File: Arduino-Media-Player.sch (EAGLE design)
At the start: 40 parts, among them IC1 AMS117-18, IC2 AMS117-33, U1 VS1053B, U2 FT232RLSSOP, U3 ATMEGA328P, U4 DS1307SO8, U5 74HC4050 LVL CONVERTER

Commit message: More minor changes
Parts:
- removed IC1: AMS117-18, SparkFun-PowerIC:V_REG_LM1117SOT223
- removed IC2: AMS117-33, SparkFun-PowerIC:V_REG_LM1117SOT223
- added U$1: MICRO-SD-CARD-EBAY, SparkFun-Connectors:MICRO-SD-CARD-EBAY
- added U6: VS1053B, SparkFun-DigitalIC:VS1033/1053SMD
- added U7: 74HC4050 LVL CONVERTER, SparkFun-DigitalIC:HEX_CONVERTER
- U1: value VS1053B -> ATMEGA328P; device SparkFun-DigitalIC:VS1033/1053SMD -> SparkFun-DigitalIC:ATMEGA328_SMT
- U3: value ATMEGA328P -> DS1307SO8; device SparkFun-DigitalIC:ATMEGA328_SMT -> SparkFun-FreqCtrl:DS1307SO8
- U4: value DS1307SO8 -> AMS117-33; device SparkFun-FreqCtrl:DS1307SO8 -> SparkFun-PowerIC:V_REG_LM1117SOT223
- U5: value 74HC4050 LVL CONVERTER -> AMS117-18; device SparkFun-DigitalIC:HEX_CONVERTER -> SparkFun-PowerIC:V_REG_LM1117SOT223
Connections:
- net /RESET: now also U1.PC6(/RESET); no longer U3.PC6(/RESET)
- net 1.8V: now also U5.OUT, U5.OUT@1, U6.CVDD1, U6.CVDD2, U6.CVDD3, U6.CVDD4; no longer IC1.OUT, IC1.OUT@1, U1.CVDD1, U1.CVDD2, U1.CVDD3, U1.CVDD4
- net 3.3V: now also U4.OUT, U4.OUT@1, U5.IN, U6.AVDD1, U6.AVDD2, U6.AVDD3, U6.IOVDD1, U6.IOVDD2, U6.IOVDD3, U6.TEST, U7.VCC; no longer IC1.IN, IC2.OUT, IC2.OUT@1, U1.AVDD1, U1.AVDD2, U1.AVDD3, U1.IOVDD1, U1.IOVDD2, U1.IOVDD3, U1.TEST, U5.VCC
- net 5V: now also U1.AREF, U1.AVCC, U1.VCC@1, U1.VCC@2, U3.VCC, U4.IN; no longer IC2.IN, U3.AREF, U3.AVCC, U3.VCC@1, U3.VCC@2, U4.VCC
- net 5V-MOSI: now also U7.1A; no longer U5.1A
- net 5V-MP3-CS: now also U7.4A; no longer U5.4A
- net 5V-MP3-DCS: now also U7.5A; no longer U5.5A
- net 5V-MP3-RST: now also U7.6A; no longer U5.6A
- net 5V-SCK: now also U7.3A; no longer U5.3A
- net 5V-SD-CS: now also U7.2A; no longer U5.2A
- net DS1307X1: now also U3.X1; no longer U4.X1
- net DS1307X2: now also U3.X2; no longer U4.X2
- net GBUF: now also U6.GBUF; no longer U1.GBUF
- net GND: now also U1.AGND, U1.GND@1, U1.GND@2, U3.GND, U4.ADJ, U5.ADJ, U6.AGND1, U6.AGND2, U6.AGND3, U6.AGND4, U6.DGND1, U6.DGND2, U6.DGND3, U6.DGND4, U6.DGND5, U6.DGND6, U7.GND; no longer IC1.ADJ, IC2.ADJ, U1.AGND1, U1.AGND2, U1.AGND3, U1.AGND4, U1.DGND1, U1.DGND2, U1.DGND3, U1.DGND4, U1.DGND5, U1.DGND6, U3.AGND, U3.GND@1, U3.GND@2, U4.GND, U5.GND
- net GPIO0: now also U6.GPIO0/I2S_SCLK; no longer U1.GPIO0/I2S_SCLK
- net GPIO1: now also U6.GPIO1/I2S_SDATA; no longer U1.GPIO1/I2S_SDATA
- net LEFT: now also U6.LEFT; no longer U1.LEFT
- net MIDI-RX: now also U6.RX; no longer U1.RX
- net MISO: now also U1.PB4(MISO), U6.S0; no longer U1.S0, U3.PB4(MISO)
- net MOSI: now also U6.SI, U7.1Y; no longer U1.SI, U5.1Y
- net MP3-CS: now also U6.XCS, U7.4Y; no longer U1.XCS, U5.4Y
- net MP3-DCS: now also U6.XDCS/BSYNC, U7.5Y; no longer U1.XDCS/BSYNC, U5.5Y
- net MP3-DREQ: now also U6.DREQ; no longer U1.DREQ
- net MP3-RST: now also U6.XRESET, U7.6Y; no longer U1.XRESET, U5.6Y
- net N$12: now also U6.GPIO5/I2C_MCLK; no longer U1.GPIO5/I2C_MCLK
- net N$13: now also U6.GPIO4/I2S_LROUT; no longer U1.GPIO4/I2S_LROUT
- net N$16: now also U6.GPIO2/DCLK, U6.GPIO3/SDATA, U6.GPIO6, U6.GPIO7; no longer U1.GPIO2/DCLK, U1.GPIO3/SDATA, U1.GPIO6, U1.GPIO7
- net N$4: now also U1.PB6(XTAL1/TOSC1); no longer U3.PB6(XTAL1/TOSC1)
- net N$5: now also U1.PB7(XTAL2/TOSC2); no longer U3.PB7(XTAL2/TOSC2)
- net RCAP: now also U6.RCAP; no longer U1.RCAP
- net RIGHT: now also U6.RIGHT; no longer U1.RIGHT
- net RXD: now also U1.PD0(RXD); no longer U3.PD0(RXD)
- net SCK: now also U6.SCLK, U7.3Y; no longer U1.SCLK, U5.3Y
- net SCL: now also U1.PC5(ADC5/SCL), U3.SCL; no longer U3.PC5(ADC5/SCL), U4.SCL
- net SD-CS: now also U7.2Y; no longer U5.2Y
- net SDA: now also U1.PC4(ADC4/SDA), U3.SDA; no longer U3.PC4(ADC4/SDA), U4.SDA
- net SQW: now also U3.SQW; no longer U4.SQW
- net TXD: now also U1.PD1(TXD); no longer U3.PD1(TXD)
- net VBATT: now also U3.VBATT; no longer U4.VBATT
- net VS1053XTAL1: now also U6.XTAL1/MCLK; no longer U1.XTAL1/MCLK
- net VS1053XTAL2: now also U6.XTAL2; no longer U1.XTAL2
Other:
- note added: "ATMEGA328P-AU (Arduino)"
- note added: "Real-Time Clock (RTC)"
- note added: "USB-to-Serial"
- moved on the sheet: C103, C108, C109, R101, R103, R104, R112, XTAL3

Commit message: update
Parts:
- removed U$1: MICRO-SD-CARD-EBAY, SparkFun-Connectors:MICRO-SD-CARD-EBAY
- added J1: MICRO-SD-CARD, SparkFun-Connectors-EDITED:MICRO-SD-CARD-EBAY
- added R102, R105, R110, R111: 100K, SparkFun-Passives:RESISTOR0805-RES
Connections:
- net 3.3V: now also J1.VCC, R102.2, R105.2
- net GND: now also J1.GND, J1.SHEILD1, J1.SHEILD2, J1.SHEILD3, J1.SHEILD4, R110.1, R111.1
- net GPIO0: now also R111.2
- net GPIO1: now also R110.2
- net MIDI-RX: now also R102.1
- net MISO: now also J1.D0
- net MOSI: now also J1.D1
- net MP3-RST: now also R105.1
- net SCK: now also J1.SCK
- net SD-CS: now also J1.CS
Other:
- moved on the sheet: C103, C108, C109, R101, R103, R104, R112, U6, XTAL3

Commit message: update
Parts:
- removed R10: 10K, rcl:R-US_R0805W
- added R5: 10K, SparkFun-Passives:RESISTOR0805-RES
- PTC1: device SparkFun-Passives:RESISTOR0805-RES -> SparkFun-Passives:PTC
- R1, R2: device rcl:R-US_R0805W -> SparkFun-Passives:RESISTOR0805-RES
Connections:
- net /RESET: now also R5.1; no longer R10.1
- net 5V: now also R5.2; no longer R10.2

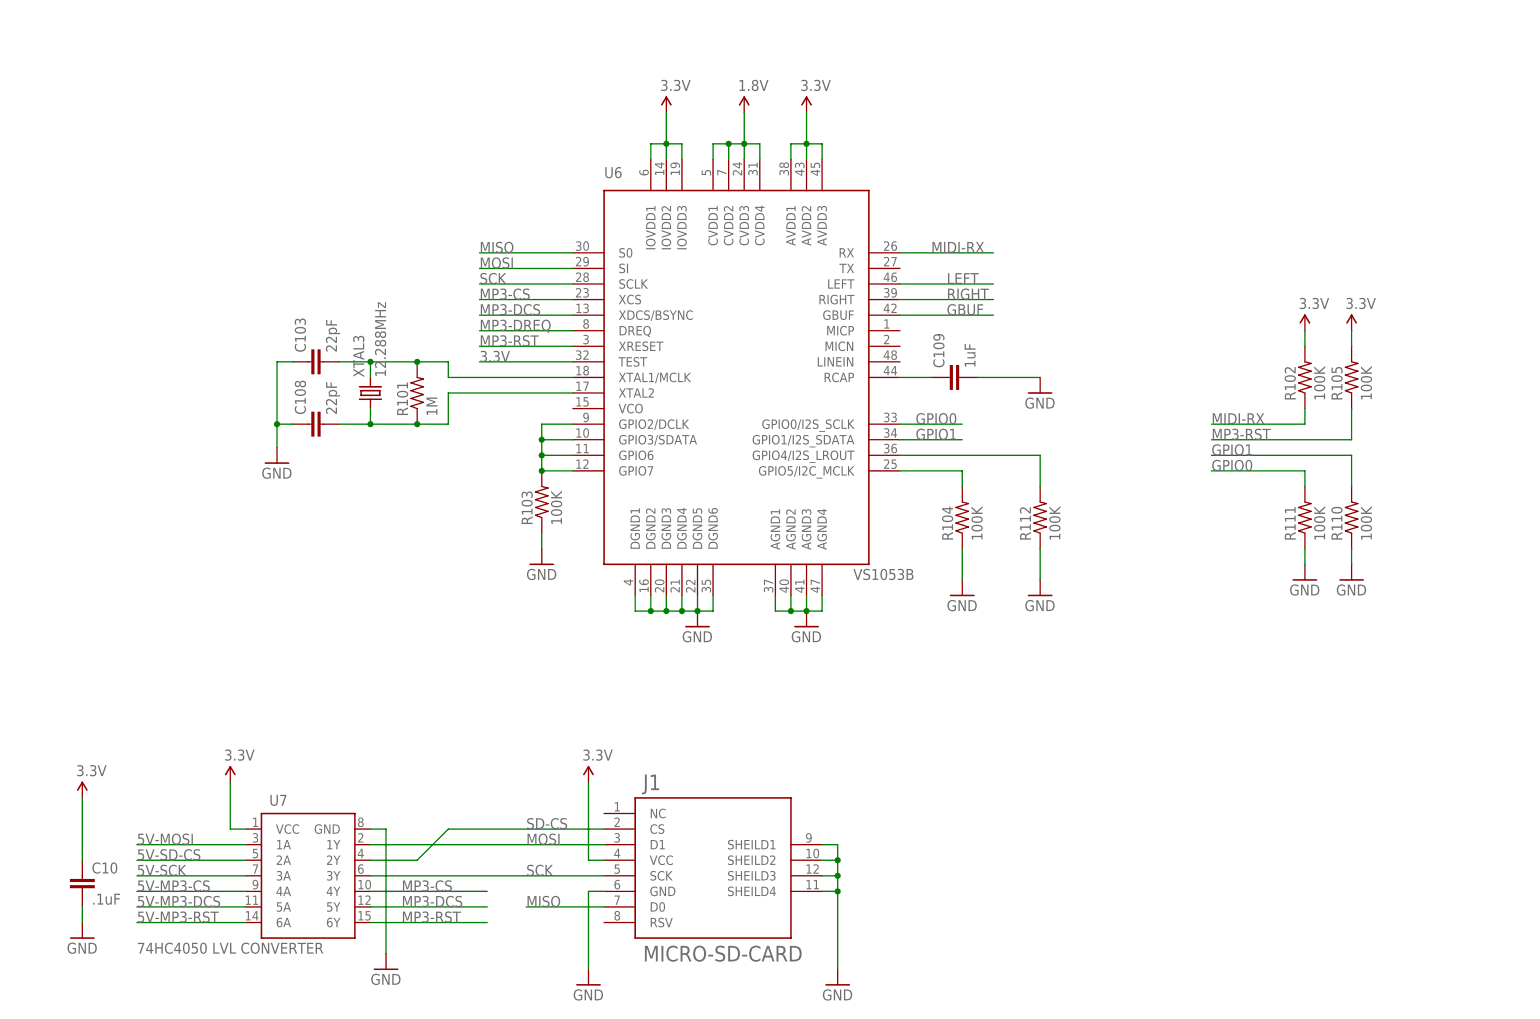
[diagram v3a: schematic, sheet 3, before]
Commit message: Added audio output circuitry for mp3 decoder
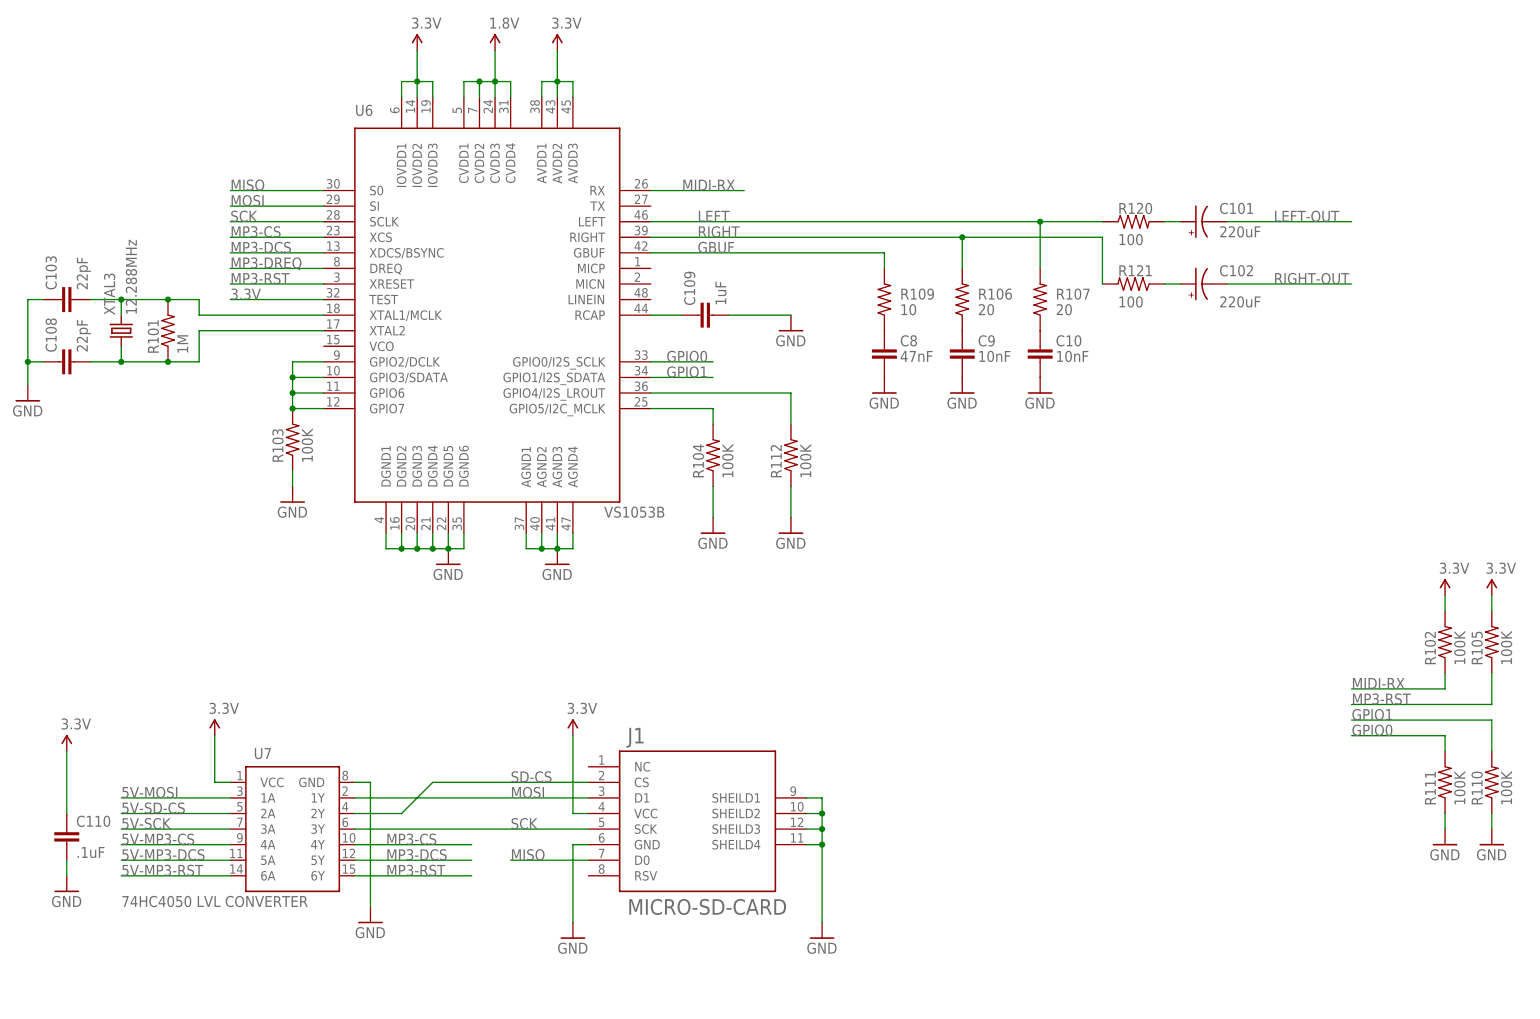
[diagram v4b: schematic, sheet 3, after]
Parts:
- added C101, C102: 220uF, SparkFun-Passives:CAP_POLG
- added C110: .1uF, SparkFun-Passives:CAP0805
- added C8: 47nF, SparkFun-Passives:CAP0805
- added C9: 10nF, SparkFun-Passives:CAP0805
- added R106, R107: 20, SparkFun-Passives:RESISTOR0805-RES
- added R109: 10, SparkFun-Passives:RESISTOR0805-RES
- added R120, R121: 100, SparkFun-Passives:RESISTOR0805-RES
- added R13, R14: 1K, SparkFun-Passives:RESISTOR0805-RES
- added SJ1, SJ2: JUMPER-PAD-2-NOROUND, SparkFun-Passives:JUMPER-PAD-2-NOROUND
- C10: value .1uF -> 10nF
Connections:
- new net 5V-GPIO1: SJ2.1, U1.PD4(XCK/T0)
- new net 5V-MIDI-RX: SJ1.1, U1.PD3(INT1)
- new net A0: U1.PC0(ADC0)
- new net A1: U1.PC1(ADC1)
- new net A2: U1.PC2(ADC2)
- new net A3: U1.PC3(ADC3)
- new net A6: U1.ADC6
- new net A7: U1.ADC7
- new net LEFT-OUT: C101.-
- new net N$1: R13.1, SJ1.2
- new net N$14: C102.+, R121.1
- new net N$15: C8.2, R109.1
- new net N$17: C9.2, R106.1
- new net N$18: C10.2, R107.1
- new net N$2: R14.1, SJ2.2
- new net N$3: C101.+, R120.2
- new net RIGHT-OUT: C102.-
- net 3.3V: now also C110.1; no longer C10.1
- net 5V-MOSI: now also U1.PB3(MOSI/OC2)
- net 5V-MP3-CS: now also U1.PD6(AIN0)
- net 5V-MP3-DCS: now also U1.PD7(AIN1)
- net 5V-MP3-RST: now also U1.PB0(ICP)
- net 5V-SCK: now also U1.PB5(SCK)
- net 5V-SD-CS: now also U1.PB1(OC1A)
- net GBUF: now also R109.2
- net GND: now also C10.1, C110.2, C8.1, C9.1; no longer C10.2
- net GPIO1: now also R14.2
- net LEFT: now also R107.2, R120.1
- net MIDI-RX: now also R13.2
- net MP3-DREQ: now also U1.PD2(INT0)
- net RIGHT: now also R106.2, R121.2
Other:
- moved on the sheet: C1, C10, C103, C108, C109, C12, C2, J1, R1, R101, R102, R103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

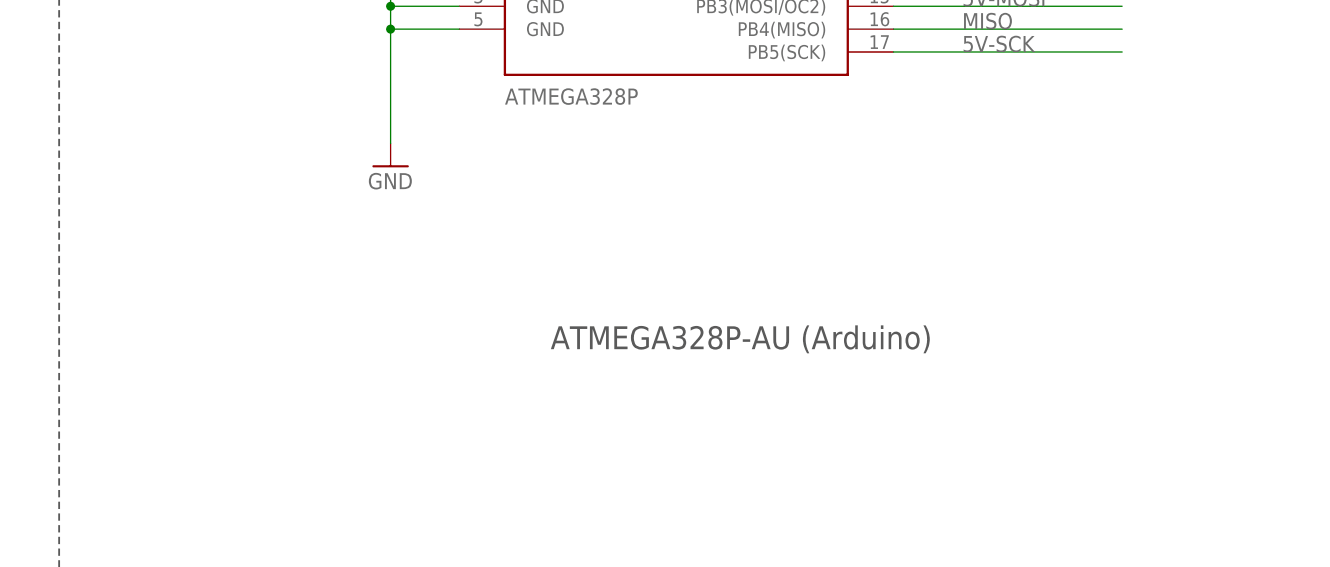
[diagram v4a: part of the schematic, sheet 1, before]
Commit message: Added ICSP header for ATMEGA328p
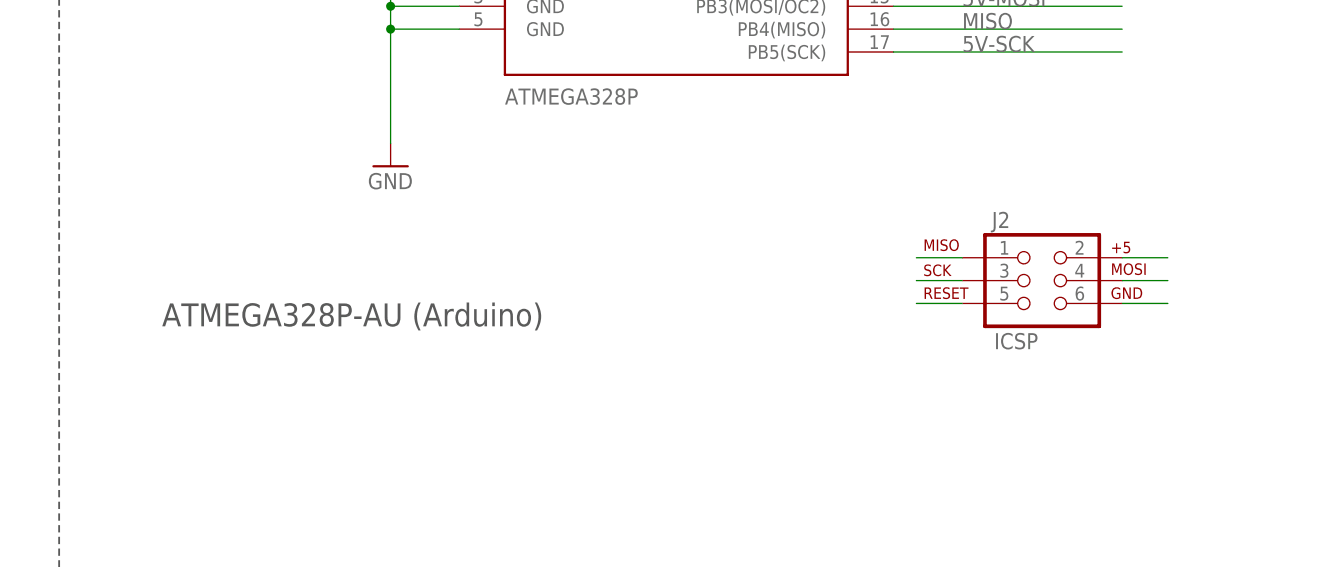
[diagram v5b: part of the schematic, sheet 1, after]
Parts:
- added J2: ICSP, SparkFun-Connectors-EDITED:AVR_SPI_PRG_6PTH
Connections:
- net /RESET: now also J2.5
- net 5V: now also J2.2
- net 5V-MOSI: now also J2.4
- net 5V-SCK: now also J2.3
- net GND: now also J2.6
- net MISO: now also J2.1
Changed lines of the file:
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@@
 <part name="GND27" library="SparkFun-Aesthetics" deviceset="GND" device=""/>
 <part name="GND28" library="SparkFun-Aesthetics" deviceset="GND" device=""/>
+<part name="J2" library="SparkFun-Connectors-EDITED" deviceset="AVR_SPI_PRG_6" device="PTH" value="ICSP"/>
 </parts>
 <sheets>
@@
 <text x="48.26" y="92.71" size="2.54" layer="97" ratio="15">USB-to-Serial</text>
 <text x="31.75" y="5.08" size="2.54" layer="97" ratio="15">Real-Time Clock (RTC)</text>
-<text x="172.72" y="33.02" size="2.54" layer="97" ratio="15">ATMEGA328P-AU (Arduino)</text>
+<text x="129.54" y="35.56" size="2.54" layer="97" ratio="15">ATMEGA328P-AU (Arduino)</text>
 </plain>
 <instances>
@@
 <attribute name="VALUE" x="247.65" y="85.598" size="1.778" layer="96"/>
 </instance>
+<instance part="J2" gate="G$1" x="226.06" y="40.64"/>
 </instances>
 <busses>
@@
 <pinref part="GND13" gate="1" pin="GND"/>
 </segment>
+<segment>
+<pinref part="J2" gate="G$1" pin="6"/>
+<wire x1="236.22" y1="38.1" x2="241.3" y2="38.1" width="0.1524" layer="91"/>
+</segment>
 </net>
 <net name="SCL" class="0">
@@
 <wire x1="160.02" y1="139.7" x2="160.02" y2="137.16" width="0.1524" layer="91"/>
 </segment>
+<segment>
+<pinref part="J2" gate="G$1" pin="2"/>
+<wire x1="236.22" y1="43.18" x2="241.3" y2="43.18" width="0.1524" layer="91"/>
+</segment>
 </net>
 <net name="SQW" class="0">
@@
 <junction x="160.02" y="124.46"/>
 </segment>
+<segment>
+<pinref part="J2" gate="G$1" pin="5"/>
+<wire x1="218.44" y1="38.1" x2="213.36" y2="38.1" width="0.1524" layer="91"/>
+</segment>
 </net>
 <net name="MISO" class="0">
@@
 <wire x1="210.82" y1="68.58" x2="236.22" y2="68.58" width="0.1524" layer="91"/>
 <label x="218.44" y="68.58" size="1.778" layer="95"/>
+</segment>
+<segment>
+<pinref part="J2" gate="G$1" pin="1"/>
+<wire x1="218.44" y1="43.18" x2="213.36" y2="43.18" width="0.1524" layer="91"/>
 </segment>
 </net>
@@
 <label x="218.44" y="71.12" size="1.778" layer="95"/>
 </segment>
+<segment>
+<pinref part="J2" gate="G$1" pin="4"/>
+<wire x1="236.22" y1="40.64" x2="241.3" y2="40.64" width="0.1524" layer="91"/>
+</segment>
 </net>
 <net name="A0" class="0">
@@
 <label x="218.44" y="66.04" size="1.778" layer="95"/>
 </segment>
-</net>
+<segment>
+<pinref part="J2" gate="G$1" pin="3"/>
+<wire x1="218.44" y1="40.64" x2="213.36" y2="40.64" width="0.1524" layer="91"/>
+</segment>
+</net>
